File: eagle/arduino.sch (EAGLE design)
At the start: 5 parts

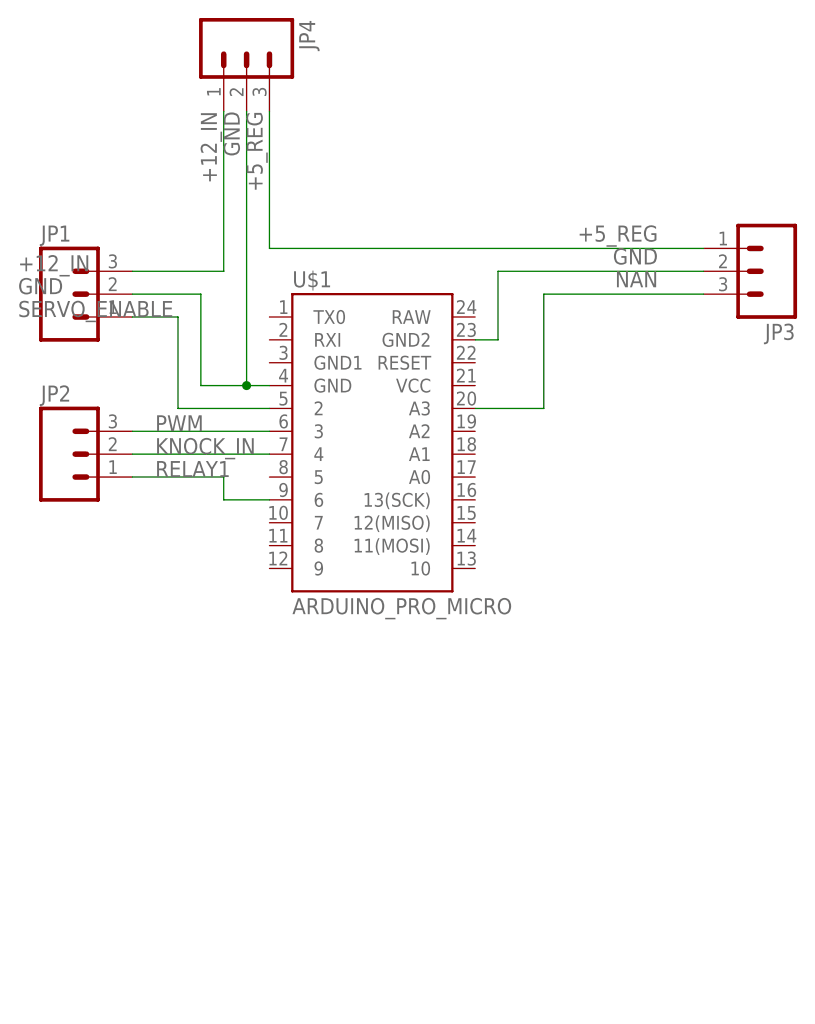
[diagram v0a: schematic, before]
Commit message: updated eagle for board revisions
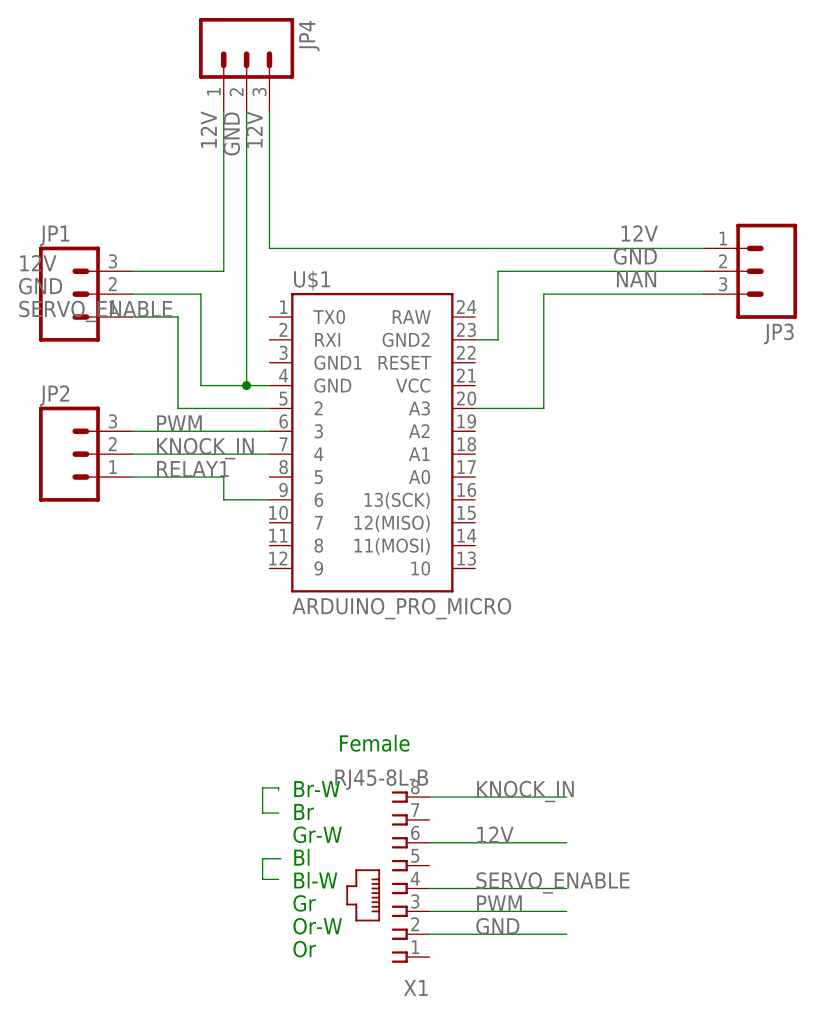
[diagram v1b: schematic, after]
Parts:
- added X1: RJ45-8L-B, con-tycoelectronics:RJ45-8L-B
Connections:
- removed net +12_IN: JP1.3, JP4.1
- removed net +5_REG: JP3.1, JP4.3
- new net 12V: JP1.3, JP3.1, JP4.1, JP4.3, X1.6
- net GND: now also X1.2
- net KNOCK_IN: now also X1.8
- net PWM: now also X1.3
- net SERVO_ENABLE: now also X1.4
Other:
- note added: "Bl"
- note added: "Bl-W"
- note added: "Br"
- note added: "Br-W"
- note added: "Female"
- note added: "Gr"
- note added: "Gr-W"
- note added: "Or"
- note added: "Or-W"
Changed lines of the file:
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@@
 <part name="JP3" library="SparkFun-Connectors" deviceset="M03" device=""/>
 <part name="JP4" library="SparkFun-Connectors" deviceset="M03" device=""/>
+<part name="X1" library="con-tycoelectronics" deviceset="RJ45" device="" technology="-8L-B"/>
 </parts>
 <sheets>
 <sheet>
 <plain>
+<text x="55.88" y="22.86" size="1.778" layer="91">Female</text>
+<text x="50.8" y="0" size="1.778" layer="91">Or</text>
+<text x="50.8" y="2.54" size="1.778" layer="91">Or-W</text>
+<text x="50.8" y="5.08" size="1.778" layer="91">Gr</text>
+<text x="50.8" y="10.16" size="1.778" layer="91">Bl</text>
+<text x="50.8" y="7.62" size="1.778" layer="91">Bl-W</text>
+<text x="50.8" y="12.7" size="1.778" layer="91">Gr-W</text>
+<text x="50.8" y="15.24" size="1.778" layer="91">Br</text>
+<text x="50.8" y="17.78" size="1.778" layer="91">Br-W</text>
 </plain>
 <instances>
@@
 <instance part="JP3" gate="G$1" x="104.14" y="76.2" rot="R180"/>
 <instance part="JP4" gate="G$1" x="45.72" y="101.6" rot="R270"/>
+<instance part="X1" gate="G$1" x="63.5" y="7.62" rot="R180"/>
 </instances>
 <busses>
@@
 <label x="20.32" y="71.12" size="1.778" layer="95"/>
 </segment>
+<segment>
+<pinref part="X1" gate="G$1" pin="4"/>
+<wire x1="66.04" y1="7.62" x2="81.28" y2="7.62" width="0.1524" layer="91"/>
+<label x="71.12" y="7.62" size="1.778" layer="95"/>
+</segment>
 </net>
 <net name="PWM" class="0">
@@
 <wire x1="33.02" y1="58.42" x2="48.26" y2="58.42" width="0.1524" layer="91"/>
 <label x="35.56" y="58.42" size="1.778" layer="95"/>
+</segment>
+<segment>
+<pinref part="X1" gate="G$1" pin="3"/>
+<wire x1="66.04" y1="5.08" x2="81.28" y2="5.08" width="0.1524" layer="91"/>
+<label x="71.12" y="5.08" size="1.778" layer="95"/>
 </segment>
 </net>
@@
 <label x="35.56" y="55.88" size="1.778" layer="95"/>
 </segment>
-</net>
-<net name="+12_IN" class="0">
 <segment>
-<pinref part="JP1" gate="G$1" pin="3"/>
-<pinref part="JP4" gate="G$1" pin="1"/>
-<wire x1="33.02" y1="76.2" x2="43.18" y2="76.2" width="0.1524" layer="91"/>
-<wire x1="43.18" y1="76.2" x2="43.18" y2="93.98" width="0.1524" layer="91"/>
-<label x="20.32" y="76.2" size="1.778" layer="95"/>
-<label x="40.64" y="93.98" size="1.778" layer="95" rot="R270"/>
-</segment>
-</net>
-<net name="+5_REG" class="0">
-<segment>
-<pinref part="JP4" gate="G$1" pin="3"/>
-<wire x1="48.26" y1="93.98" x2="48.26" y2="78.74" width="0.1524" layer="91"/>
-<pinref part="JP3" gate="G$1" pin="1"/>
-<wire x1="48.26" y1="78.74" x2="96.52" y2="78.74" width="0.1524" layer="91"/>
-<label x="45.72" y="93.98" size="1.778" layer="95" rot="R270"/>
-<label x="91.44" y="81.28" size="1.778" layer="95" rot="R180"/>
+<pinref part="X1" gate="G$1" pin="8"/>
+<wire x1="66.04" y1="17.78" x2="81.28" y2="17.78" width="0.1524" layer="91"/>
+<label x="71.12" y="17.78" size="1.778" layer="95"/>
 </segment>
 </net>
@@
 <label x="43.18" y="93.98" size="1.778" layer="95" rot="R270"/>
 </segment>
+<segment>
+<pinref part="X1" gate="G$1" pin="2"/>
+<wire x1="66.04" y1="2.54" x2="81.28" y2="2.54" width="0.1524" layer="91"/>
+<label x="71.12" y="2.54" size="1.778" layer="95"/>
+</segment>
 </net>
 <net name="NAN" class="0">
@@
 </segment>
 </net>
+<net name="N$1" class="0">
+<segment>
+<wire x1="49.276" y1="8.636" x2="47.498" y2="8.636" width="0.2032" layer="91"/>
+<wire x1="47.498" y1="8.636" x2="47.498" y2="10.922" width="0.2032" layer="91"/>
+<wire x1="47.498" y1="10.922" x2="49.53" y2="10.922" width="0.2032" layer="91"/>
+</segment>
+</net>
+<net name="N$2" class="0">
+<segment>
+<wire x1="49.276" y1="16.002" x2="47.498" y2="16.002" width="0.2032" layer="91"/>
+<wire x1="47.498" y1="16.002" x2="47.498" y2="18.796" width="0.2032" layer="91"/>
+<wire x1="47.498" y1="18.796" x2="49.276" y2="18.796" width="0.2032" layer="91"/>
+<wire x1="49.276" y1="18.796" x2="49.276" y2="18.542" width="0.2032" layer="91"/>
+</segment>
+</net>
+<net name="12V" class="0">
+<segment>
+<pinref part="X1" gate="G$1" pin="6"/>
+<wire x1="66.04" y1="12.7" x2="81.28" y2="12.7" width="0.1524" layer="91"/>
+<label x="71.12" y="12.7" size="1.778" layer="95"/>
+</segment>
+<segment>
+<pinref part="JP4" gate="G$1" pin="3"/>
+<wire x1="48.26" y1="93.98" x2="48.26" y2="78.74" width="0.1524" layer="91"/>
+<pinref part="JP3" gate="G$1" pin="1"/>
+<wire x1="48.26" y1="78.74" x2="96.52" y2="78.74" width="0.1524" layer="91"/>
+<label x="45.72" y="93.98" size="1.778" layer="95" rot="R270"/>
+<label x="91.44" y="81.28" size="1.778" layer="95" rot="R180"/>
+</segment>
+<segment>
+<pinref part="JP1" gate="G$1" pin="3"/>
+<pinref part="JP4" gate="G$1" pin="1"/>
+<wire x1="33.02" y1="76.2" x2="43.18" y2="76.2" width="0.1524" layer="91"/>
+<wire x1="43.18" y1="76.2" x2="43.18" y2="93.98" width="0.1524" layer="91"/>
+<label x="20.32" y="76.2" size="1.778" layer="95"/>
+<label x="40.64" y="93.98" size="1.778" layer="95" rot="R270"/>
+</segment>
+</net>
